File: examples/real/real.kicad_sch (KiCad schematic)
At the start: 1 part

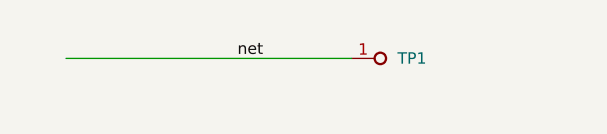
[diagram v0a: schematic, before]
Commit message: Huge rewrite to enhance functionality and fix some limitations
- Allow for selection of input and output folders.
- Added settings for:
    - Adjusting xy offset of port positions.
    - Settings to control nanomesh quality when converting gerbers to images.
    - Unified 0 indexing for simulation ports in KiCAD schematic and python scripts.
    - Allow adjusting smoothing ratio for mesh lines.
    - Stackup layers moved from separate "fab/stackup.json" to inside "simulation.json".
    - Backup gerber files and simulation.json config inside simulation output to keep track of parametric search changes in schematic.
    - Output visualisation of gerber to image mesh for debugging semi-buggy nanomesh workflow where there will be unwanted merging of nets.
    - Added option for dielectric layers to use a gerber file as mesh.
    - Added option to repeat layer for given z-heights.
- Fixed examples/* to reflect modifications to gerber2ems.
- Added examples/differential_hatched as additional example.
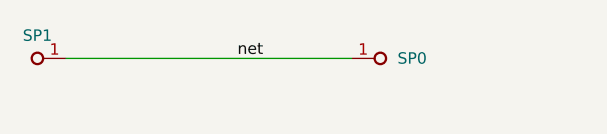
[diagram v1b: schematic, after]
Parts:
- added SP1: Simulation_Port, NetTie:NetTie-2_SMD_Pad0.5mm, symbol antmicroTestPoints:TP_0.75mm_SMD
- SP0: renamed from TP1; value TP_0.75mm_SMD -> Simulation_Port; footprint antmicro-footprints:TP_SMD_0.75mm -> NetTie:NetTie-2_SMD_Pad0.5mm
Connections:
- net net: now also SP1.1

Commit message: Update examples with corrected settings and keep track of exported gerbers
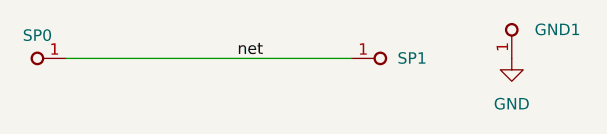
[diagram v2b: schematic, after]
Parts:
- added GND1: GND, simulation_port:pad_0.1mm, symbol antmicroTestPoints:TP_0.75mm_SMD
- SP0: renamed from SP1; footprint NetTie:NetTie-2_SMD_Pad0.5mm -> simulation_port:pad_0.2mm
- SP1: renamed from SP0; footprint NetTie:NetTie-2_SMD_Pad0.5mm -> simulation_port:pad_0.2mm
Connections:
- new net GND: GND1.1
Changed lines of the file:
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@@
 		(dnp no)
 		(fields_autoplaced yes)
-		(property "Reference" "SP0"
+		(property "Reference" "SP1"
 			(at 184.15 81.28 0)
 			(effects
@@
 			)
 		)
-		(property "Footprint" "NetTie:NetTie-2_SMD_Pad0.5mm"
+		(property "Footprint" "simulation_port:pad_0.2mm"
 			(at 189.865 87.63 0)
 			(effects
@@
 			(project "real"
 				(path "/eecc7681-2412-442b-9517-c501f47b009c"
-					(reference "SP0")
+					(reference "SP1")
+					(unit 1)
+				)
+			)
+		)
+	)
+	(symbol
+		(lib_id "power:GND")
+		(at 196.85 81.28 0)
+		(unit 1)
+		(exclude_from_sim no)
+		(in_bom yes)
+		(on_board yes)
+		(dnp no)
+		(fields_autoplaced yes)
+		(property "Reference" "#PWR01"
+			(at 196.85 87.63 0)
+			(effects
+				(font
+					(size 1.27 1.27)
+				)
+				(hide yes)
+			)
+		)
+		(property "Value" "GND"
+			(at 196.85 86.36 0)
+			(effects
+				(font
+					(size 1.27 1.27)
+				)
+			)
+		)
+		(property "Footprint" ""
+			(at 196.85 81.28 0)
+			(effects
+				(font
+					(size 1.27 1.27)
+				)
+				(hide yes)
+			)
+		)
+		(property "Datasheet" ""
+			(at 196.85 81.28 0)
+			(effects
+				(font
+					(size 1.27 1.27)
+				)
+				(hide yes)
+			)
+		)
+		(property "Description" "Power symbol creates a global label with name \"GND\" , ground"
+			(at 196.85 81.28 0)
+			(effects
+				(font
+					(size 1.27 1.27)
+				)
+				(hide yes)
+			)
+		)
+		(pin "1"
+		)
+		(instances
+			(project ""
+				(path "/eecc7681-2412-442b-9517-c501f47b009c"
+					(reference "#PWR01")
 					(unit 1)
 				)
@@
 		(dnp no)
 		(fields_autoplaced yes)
-		(property "Reference" "SP1"
+		(property "Reference" "SP0"
 			(at 144.145 78.74 0)
 			(effects
@@
 			)
 		)
-		(property "Footprint" "NetTie:NetTie-2_SMD_Pad0.5mm"
+		(property "Footprint" "simulation_port:pad_0.2mm"
 			(at 136.525 74.93 0)
 			(effects
@@
 			(project "real"
 				(path "/eecc7681-2412-442b-9517-c501f47b009c"
-					(reference "SP1")
+					(reference "SP0")
 					(unit 1)
 				)
+			)
+		)
+	)
+	(symbol
+		(lib_id "antmicroTestPoints:TP_0.75mm_SMD")
+		(at 196.85 81.28 90)
+		(unit 1)
+		(exclude_from_sim no)
+		(in_bom no)
+		(on_board yes)
+		(dnp no)
+		(fields_autoplaced yes)
+		(property "Reference" "GND1"
+			(at 199.39 78.105 90)
+			(effects
+				(font
+					(size 1.27 1.27)
+					(thickness 0.15)
+				)
+				(justify right)
+			)
+		)
+		(property "Value" "GND"
+			(at 200.66 70.485 0)
+			(effects
+				(font
+					(size 1.27 1.27)
+					(thickness 0.15)
+				)
+				(justify left bottom)
+				(hide yes)
+			)
+		)
+		(property "Footprint" "simulation_port:pad_0.1mm"
+			(at 203.2 70.485 0)
+			(effects
+				(font
+					(size 1.27 1.27)
+					(thickness 0.15)
+				)
+				(justify left bottom)
+				(hide yes)
+			)
+		)
+		(property "Datasheet" ""
+			(at 209.55 63.5 0)
+			(effects
+				(font
+					(size 1.27 1.27)
+					(thickness 0.15)
+				)
+				(justify left bottom)
+				(hide yes)
+			)
+		)
+		(property "Description" ""
+			(at 196.85 81.28 0)
+			(effects
+				(font
+					(size 1.27 1.27)
+				)
+				(hide yes)
+			)
+		)
+		(property "MPN" ""
+			(at 208.28 70.485 0)
+			(effects
+				(font
+					(size 1.27 1.27)
+					(thickness 0.15)
+				)
+				(justify left bottom)
+				(hide yes)
+			)
+		)
+		(property "Manufacturer" ""
+			(at 203.2 70.485 0)
+			(effects
+				(font
+					(size 1.27 1.27)
+					(thickness 0.15)
+				)
+				(justify left bottom)
+				(hide yes)
+			)
+		)
+		(property "Author" "Antmicro"
+			(at 205.74 70.485 0)
+			(effects
+				(font
+					(size 1.27 1.27)
+					(thickness 0.15)
+				)
+				(justify left bottom)
+				(hide yes)
+			)
+		)
+		(property "License" "Apache-2.0"
+			(at 208.28 70.485 0)
+			(effects
+				(font
+					(size 1.27 1.27)
+					(thickness 0.15)
+				)
+				(justify left bottom)
+				(hide yes)
+			)
+		)
+		(pin "1"
+		)
+		(instances
+			(project "real"
+				(path "/eecc7681-2412-442b-9517-c501f47b009c"
+					(reference "GND1")
+					(unit 1)
+				)
